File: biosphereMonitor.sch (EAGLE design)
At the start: 42 parts, among them IC1 XMEGA32A4AU, IC2 LM35, IC3 FT232RL, Q1 16Mhz, Q2 32kHz

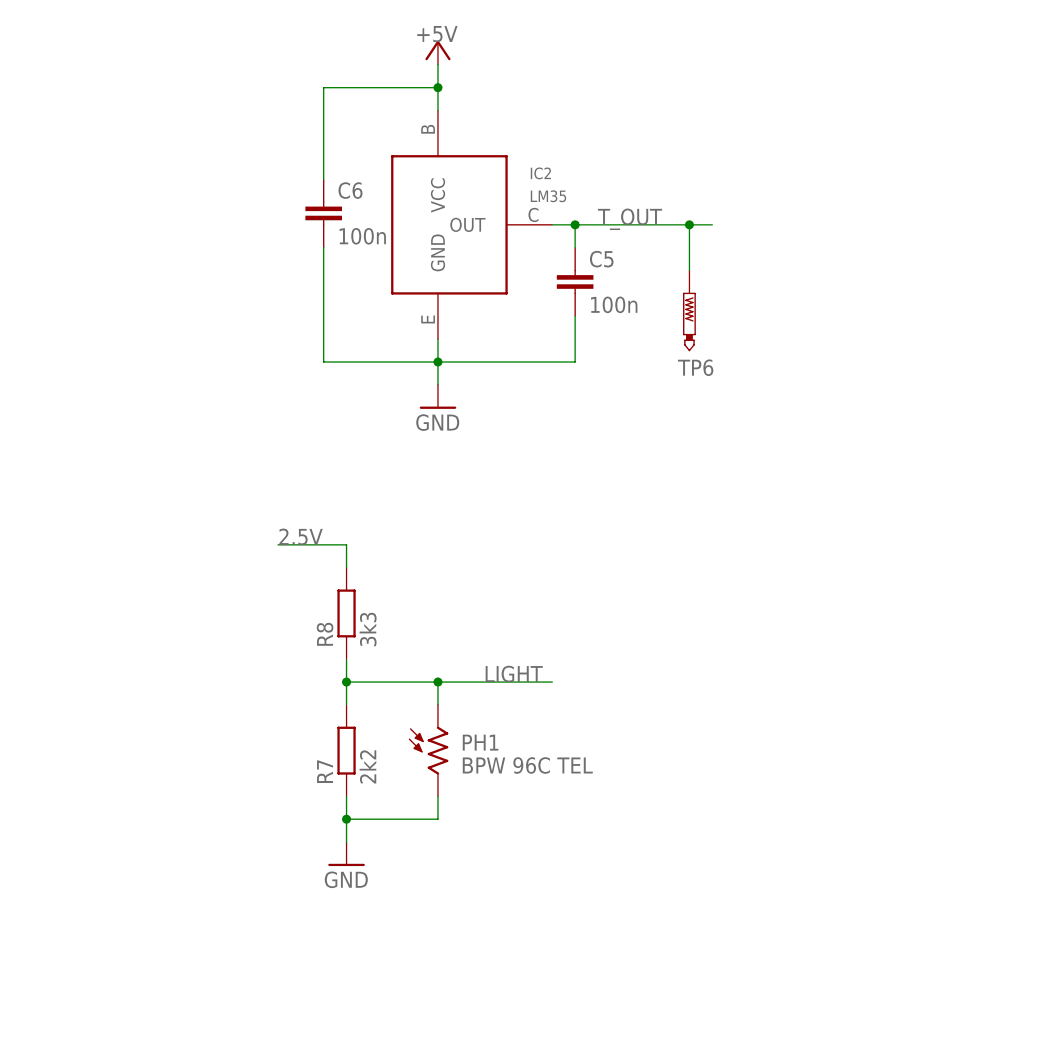
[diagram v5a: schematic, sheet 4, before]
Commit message: changed light Sensor to frequency Messurment
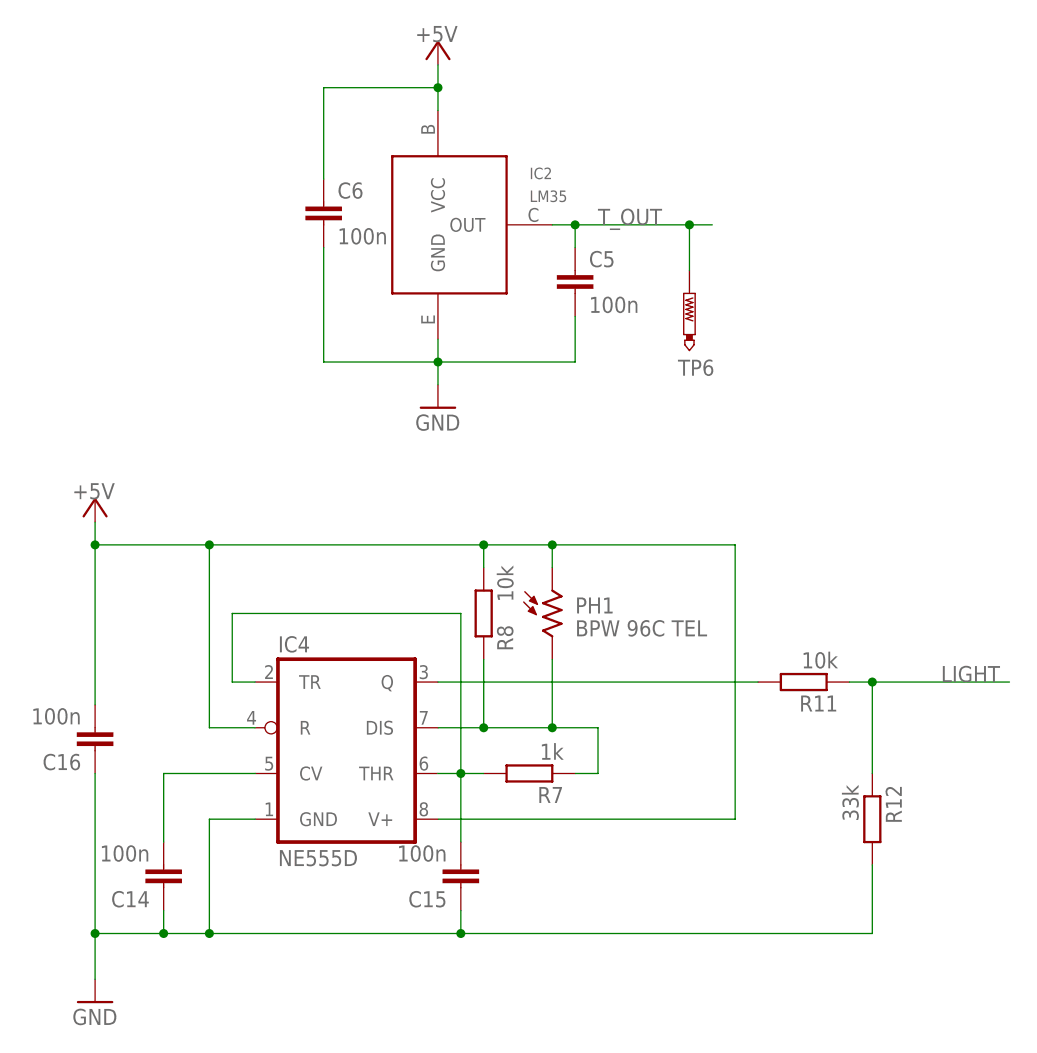
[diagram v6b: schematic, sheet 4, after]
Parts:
- added C14, C15, C16: 100n, rcl:C-EUC0805
- added IC4: NE555D, linear:NE555D
- added R11: 10k, rcl:R-EU_R0805
- added R12: 33k, rcl:R-EU_R0805
- R7: value 2k2 -> 1k
- R8: value 3k3 -> 10k
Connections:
- new net N$21: IC4.DIS, PH1.2, R7.1, R8.2
- new net N$22: C14.1, IC4.CV
- new net N$23: C15.1, IC4.THR, IC4.TR, R7.2
- new net N$24: IC4.Q, R11.2
- net +5V: now also C16.1, IC4.R, IC4.V+, PH1.1, R8.1
- net 2.5V: no longer R8.2
- net GND: now also C14.2, C15.2, C16.2, IC4.GND, R12.2; no longer PH1.2, R7.1
- net LIGHT: now also IC1.PD5, R11.1, R12.1; no longer IC1.PA1, PH1.1, R7.2, R8.1
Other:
- moved on the sheet: PH1, R7, R8

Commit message: added lux messurment
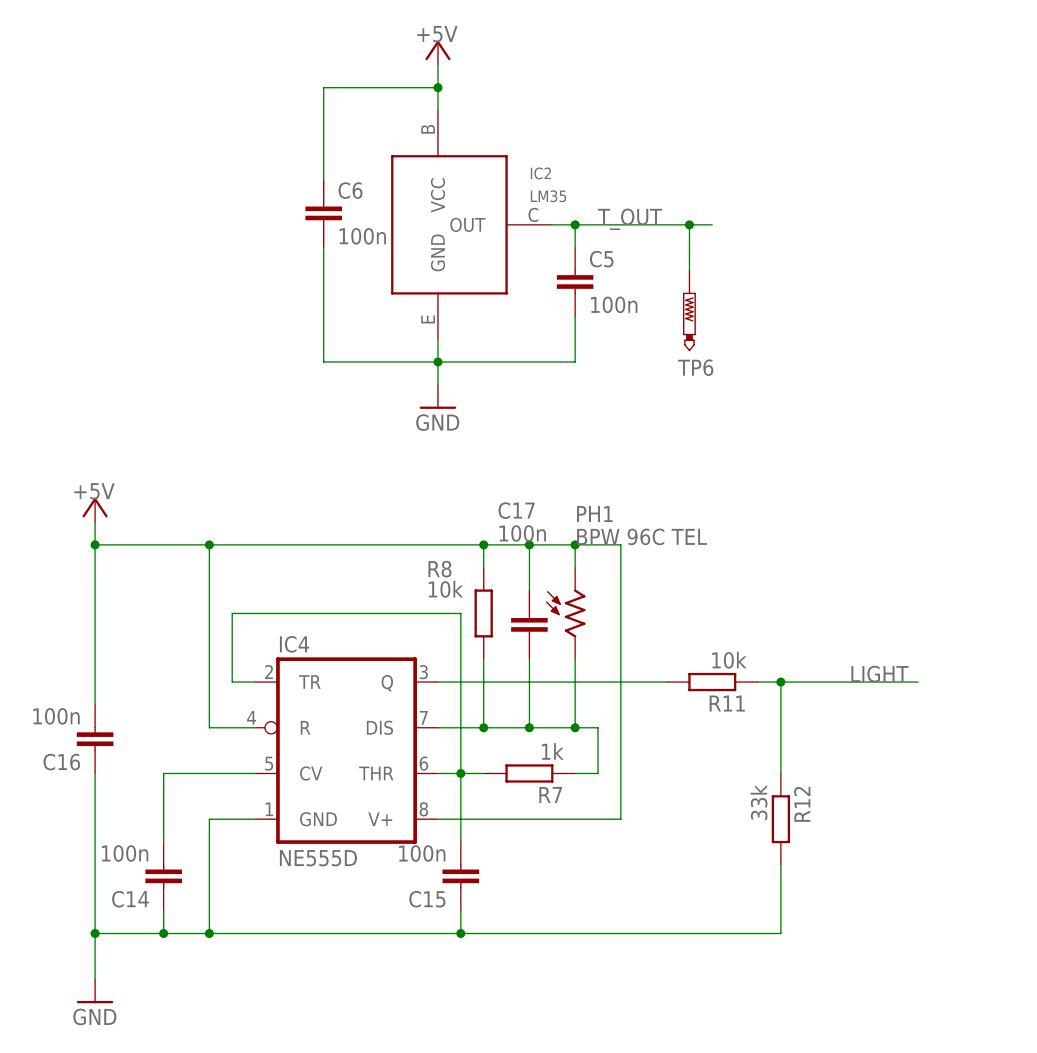
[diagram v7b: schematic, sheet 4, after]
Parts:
- added C17: 100n, rcl:C-EUC0805
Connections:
- net +5V: now also C17.1
- net N$21: now also C17.2
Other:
- moved on the sheet: PH1, R11, R12
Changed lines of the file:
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@@
 <part name="R11" library="rcl" library_urn="urn:adsk.eagle:library:334" deviceset="R-EU_" device="R0805" package3d_urn="urn:adsk.eagle:package:23553/2" value="10k"/>
 <part name="R12" library="rcl" library_urn="urn:adsk.eagle:library:334" deviceset="R-EU_" device="R0805" package3d_urn="urn:adsk.eagle:package:23553/2" value="33k"/>
+<part name="C17" library="rcl" library_urn="urn:adsk.eagle:library:334" deviceset="C-EU" device="C0805" package3d_urn="urn:adsk.eagle:package:23617/2" value="100n"/>
 </parts>
 <sheets>
@@
 <attribute name="TP_SIGNAL_NAME" x="29.21" y="30.48" size="1.778" layer="97"/>
 </instance>
-<instance part="PH1" gate="G$1" x="12.7" y="-2.54" smashed="yes">
-<attribute name="NAME" x="15.24" y="-2.54" size="1.778" layer="95"/>
-<attribute name="VALUE" x="15.24" y="-5.08" size="1.778" layer="96"/>
+<instance part="PH1" gate="G$1" x="15.24" y="-2.54" smashed="yes">
+<attribute name="NAME" x="15.24" y="7.62" size="1.778" layer="95"/>
+<attribute name="VALUE" x="15.24" y="5.08" size="1.778" layer="96"/>
 </instance>
 <instance part="IC4" gate="A" x="-10.16" y="-17.78" smashed="yes">
@@
 </instance>
 <instance part="R8" gate="G$1" x="5.08" y="-2.54" smashed="yes" rot="R270">
-<attribute name="NAME" x="6.5786" y="-3.81" size="1.778" layer="95" rot="R270"/>
-<attribute name="VALUE" x="8.382" y="-1.27" size="1.778" layer="96" rot="R90"/>
-</instance>
-<instance part="R11" gate="G$1" x="40.64" y="-10.16" smashed="yes" rot="R180">
-<attribute name="NAME" x="44.45" y="-11.6586" size="1.778" layer="95" rot="R180"/>
-<attribute name="VALUE" x="44.45" y="-6.858" size="1.778" layer="96" rot="R180"/>
-</instance>
-<instance part="R12" gate="G$1" x="48.26" y="-25.4" smashed="yes" rot="R270">
-<attribute name="NAME" x="49.7586" y="-21.59" size="1.778" layer="95" rot="R270"/>
-<attribute name="VALUE" x="44.958" y="-21.59" size="1.778" layer="96" rot="R270"/>
+<attribute name="NAME" x="-1.27" y="1.4986" size="1.778" layer="95"/>
+<attribute name="VALUE" x="-1.27" y="-0.762" size="1.778" layer="96"/>
+</instance>
+<instance part="R11" gate="G$1" x="30.48" y="-10.16" smashed="yes" rot="R180">
+<attribute name="NAME" x="34.29" y="-11.6586" size="1.778" layer="95" rot="R180"/>
+<attribute name="VALUE" x="34.29" y="-6.858" size="1.778" layer="96" rot="R180"/>
+</instance>
+<instance part="R12" gate="G$1" x="38.1" y="-25.4" smashed="yes" rot="R270">
+<attribute name="NAME" x="39.5986" y="-21.59" size="1.778" layer="95" rot="R270"/>
+<attribute name="VALUE" x="34.798" y="-21.59" size="1.778" layer="96" rot="R270"/>
+</instance>
+<instance part="C17" gate="G$1" x="10.16" y="-2.54" smashed="yes">
+<attribute name="NAME" x="6.604" y="8.001" size="1.778" layer="95"/>
+<attribute name="VALUE" x="6.604" y="5.461" size="1.778" layer="96"/>
 </instance>
 </instances>
@@
 <junction x="-38.1" y="-38.1"/>
 <pinref part="R12" gate="G$1" pin="2"/>
-<wire x1="48.26" y1="-30.48" x2="48.26" y2="-38.1" width="0.1524" layer="91"/>
-<wire x1="48.26" y1="-38.1" x2="2.54" y2="-38.1" width="0.1524" layer="91"/>
+<wire x1="38.1" y1="-30.48" x2="38.1" y2="-38.1" width="0.1524" layer="91"/>
+<wire x1="38.1" y1="-38.1" x2="2.54" y2="-38.1" width="0.1524" layer="91"/>
 <junction x="2.54" y="-38.1"/>
 </segment>
@@
 <segment>
 <pinref part="IC4" gate="A" pin="V+"/>
-<wire x1="0" y1="-25.4" x2="33.02" y2="-25.4" width="0.1524" layer="91"/>
-<wire x1="33.02" y1="-25.4" x2="33.02" y2="5.08" width="0.1524" layer="91"/>
-<wire x1="33.02" y1="5.08" x2="12.7" y2="5.08" width="0.1524" layer="91"/>
-<wire x1="12.7" y1="5.08" x2="5.08" y2="5.08" width="0.1524" layer="91"/>
+<wire x1="0" y1="-25.4" x2="20.32" y2="-25.4" width="0.1524" layer="91"/>
+<wire x1="20.32" y1="-25.4" x2="20.32" y2="5.08" width="0.1524" layer="91"/>
+<wire x1="20.32" y1="5.08" x2="15.24" y2="5.08" width="0.1524" layer="91"/>
+<wire x1="15.24" y1="5.08" x2="10.16" y2="5.08" width="0.1524" layer="91"/>
 <pinref part="IC4" gate="A" pin="R"/>
+<wire x1="10.16" y1="5.08" x2="5.08" y2="5.08" width="0.1524" layer="91"/>
 <wire x1="5.08" y1="5.08" x2="-25.4" y2="5.08" width="0.1524" layer="91"/>
 <wire x1="-20.32" y1="-15.24" x2="-25.4" y2="-15.24" width="0.1524" layer="91"/>
@@
 <junction x="-25.4" y="5.08"/>
 <pinref part="PH1" gate="G$1" pin="1"/>
-<wire x1="12.7" y1="2.54" x2="12.7" y2="5.08" width="0.1524" layer="91"/>
-<junction x="12.7" y="5.08"/>
+<wire x1="15.24" y1="2.54" x2="15.24" y2="5.08" width="0.1524" layer="91"/>
+<junction x="15.24" y="5.08"/>
 <pinref part="C16" gate="G$1" pin="1"/>
 <wire x1="-38.1" y1="-12.7" x2="-38.1" y2="5.08" width="0.1524" layer="91"/>
@@
 <wire x1="5.08" y1="2.54" x2="5.08" y2="5.08" width="0.1524" layer="91"/>
 <junction x="5.08" y="5.08"/>
+<pinref part="C17" gate="G$1" pin="1"/>
+<wire x1="10.16" y1="0" x2="10.16" y2="5.08" width="0.1524" layer="91"/>
+<junction x="10.16" y="5.08"/>
 </segment>
 </net>
 <net name="LIGHT" class="0">
 <segment>
-<label x="55.88" y="-10.16" size="1.778" layer="95"/>
-<wire x1="45.72" y1="-10.16" x2="48.26" y2="-10.16" width="0.1524" layer="91"/>
+<label x="45.72" y="-10.16" size="1.778" layer="95"/>
+<wire x1="35.56" y1="-10.16" x2="38.1" y2="-10.16" width="0.1524" layer="91"/>
 <pinref part="R11" gate="G$1" pin="1"/>
 <pinref part="R12" gate="G$1" pin="1"/>
-<wire x1="48.26" y1="-10.16" x2="63.5" y2="-10.16" width="0.1524" layer="91"/>
-<wire x1="48.26" y1="-20.32" x2="48.26" y2="-10.16" width="0.1524" layer="91"/>
-<junction x="48.26" y="-10.16"/>
+<wire x1="38.1" y1="-10.16" x2="53.34" y2="-10.16" width="0.1524" layer="91"/>
+<wire x1="38.1" y1="-20.32" x2="38.1" y2="-10.16" width="0.1524" layer="91"/>
+<junction x="38.1" y="-10.16"/>
 </segment>
 </net>
@@
 <pinref part="PH1" gate="G$1" pin="2"/>
 <wire x1="0" y1="-15.24" x2="5.08" y2="-15.24" width="0.1524" layer="91"/>
-<wire x1="5.08" y1="-15.24" x2="12.7" y2="-15.24" width="0.1524" layer="91"/>
-<wire x1="12.7" y1="-15.24" x2="12.7" y2="-7.62" width="0.1524" layer="91"/>
+<wire x1="5.08" y1="-15.24" x2="10.16" y2="-15.24" width="0.1524" layer="91"/>
+<wire x1="10.16" y1="-15.24" x2="15.24" y2="-15.24" width="0.1524" layer="91"/>
+<wire x1="15.24" y1="-15.24" x2="15.24" y2="-7.62" width="0.1524" layer="91"/>
 <pinref part="R7" gate="G$1" pin="1"/>
 <wire x1="15.24" y1="-20.32" x2="17.78" y2="-20.32" width="0.1524" layer="91"/>
 <wire x1="17.78" y1="-20.32" x2="17.78" y2="-15.24" width="0.1524" layer="91"/>
-<wire x1="17.78" y1="-15.24" x2="12.7" y2="-15.24" width="0.1524" layer="91"/>
-<junction x="12.7" y="-15.24"/>
+<wire x1="17.78" y1="-15.24" x2="15.24" y2="-15.24" width="0.1524" layer="91"/>
+<junction x="15.24" y="-15.24"/>
 <pinref part="R8" gate="G$1" pin="2"/>
 <wire x1="5.08" y1="-7.62" x2="5.08" y2="-15.24" width="0.1524" layer="91"/>
 <junction x="5.08" y="-15.24"/>
+<pinref part="C17" gate="G$1" pin="2"/>
+<wire x1="10.16" y1="-7.62" x2="10.16" y2="-15.24" width="0.1524" layer="91"/>
+<junction x="10.16" y="-15.24"/>
 </segment>
 </net>
@@
 <segment>
 <pinref part="IC4" gate="A" pin="Q"/>
-<wire x1="0" y1="-10.16" x2="35.56" y2="-10.16" width="0.1524" layer="91"/>
+<wire x1="0" y1="-10.16" x2="25.4" y2="-10.16" width="0.1524" layer="91"/>
 <pinref part="R11" gate="G$1" pin="2"/>
 </segment>

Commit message: added humidity conversion to percent and completed schematic
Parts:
- added BT!: CR2032, Tjarks_Bauteile (1):CR2032
- added C18: 100n, rcl:C-EUC0805
- added D2: 1N4148, diode:DIODE-MINIMELF
- added IC5: SST25VF040, Tjarks_Bauteile (1):SST25VF040SO08W
- added JP5: (no value), jumper:JP1E
- added R13: 22k, rcl:R-EU_R0805
- added R14: 10k, rcl:R-EU_R0805
- added TP7, TP8: PTR1B2,54, testpad:PTR1B2,54
- R10: value 3k3 -> 33k
- R9: value 2k2 -> 22k
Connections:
- new net MEM_CE: IC1.PC4, IC5.CE
- new net MEM_HOLD: IC1.PD0, IC5.HOLD
- new net MEM_MISO: IC1.PC6, IC5.SO
- new net MEM_MOSI: IC1.PC5, IC5.SI
- new net MEM_SCK: IC1.PC7, IC5.SCK
- new net MEM_WP: IC1.PD1, IC5.WP
- new net N$25: JP4.1, R13.1
- new net N$26: BT!.+, JP5.1
- new net N$27: D2.A, JP5.2
- net +3V3: now also C18.2, D2.C, IC5.VCC
- net GND: now also BT!.-, C18.1, IC5.VSS, R14.2
- net LIGHT: now also TP7.TP
- net SOIL: now also R13.2, R14.1, TP8.TP; no longer JP4.1
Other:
- moved on the sheet: R4, R5, TP3, TP4, TP5
